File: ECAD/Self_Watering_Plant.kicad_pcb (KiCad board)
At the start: 2 copper layers, 65 parts, among them J1 Conn_01x02, J2 Conn_01x02, J3 Conn_01x02, J4 Conn_01x02, J5 Conn_01x02, J6 USB_A, J7 Conn_01x02, J8 Conn_01x02, J9 Conn_01x03, P1 U262-161N-4BVC11, Q1 BC817, Q2 BC817, Q3 NCE3018AS, Q4 NCE3018AS, Q5 NCE3018AS, Q6 NCE3018AS, Q7 NCE3018AS, Q8 NCE3018AS, Q9 TEPT4400, SW1 SW_Push, U1 LM293, U10 DHT11, U3 CH340C, U4 ESP32-WROOM-32, U5 NC7SB3157P6X, U6 NC7SB3157P6X, U7 NC7SB3157P6X, U8 LM293

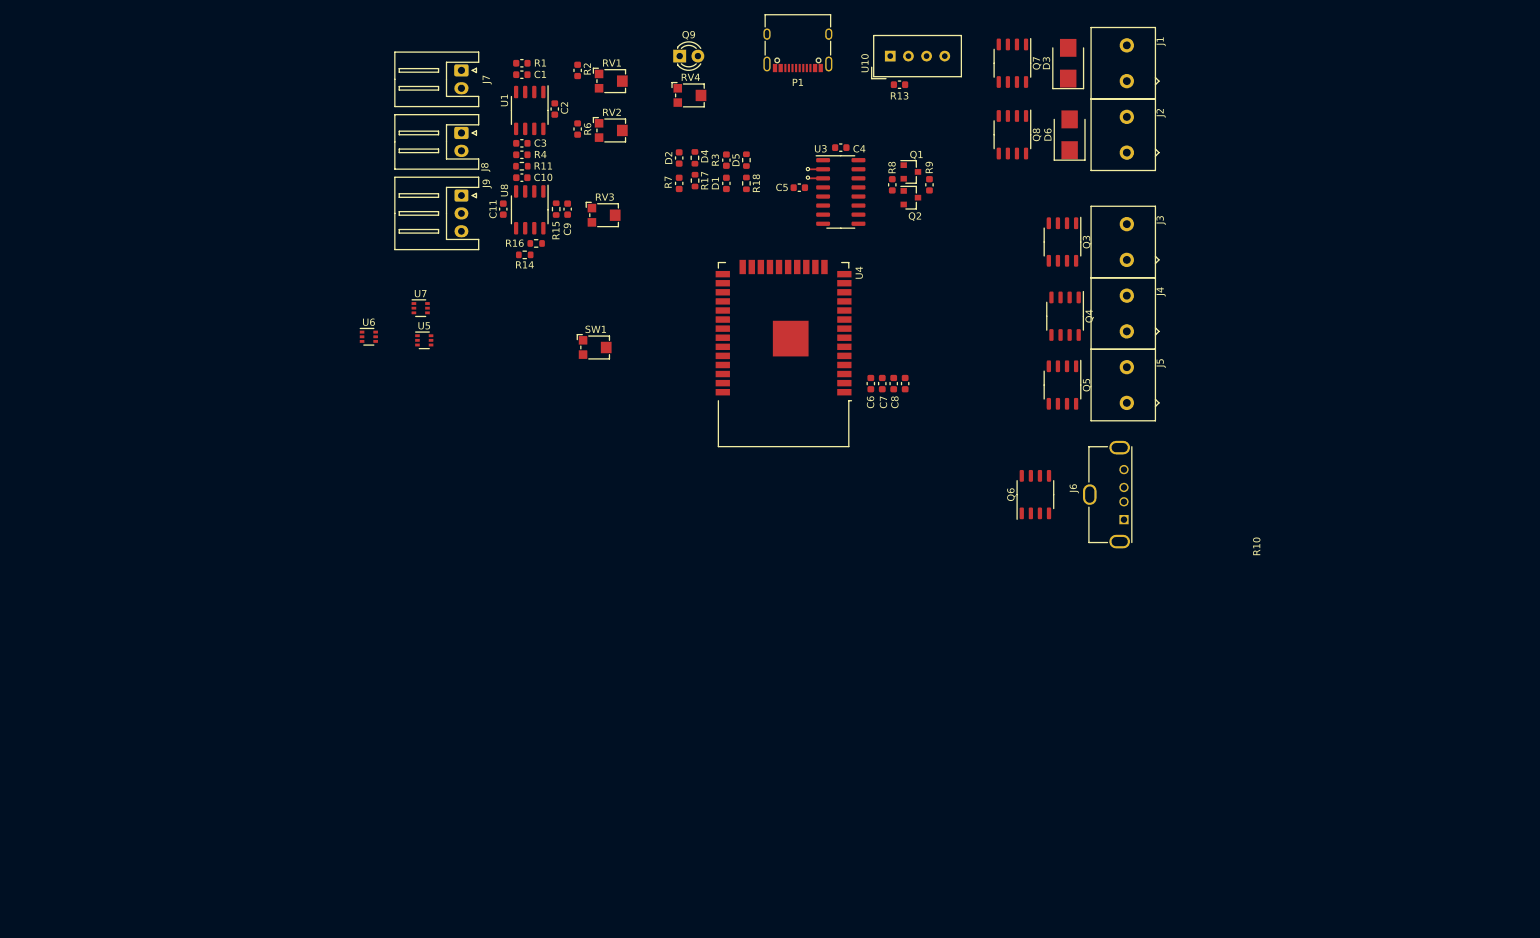
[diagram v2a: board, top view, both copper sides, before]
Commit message: finishing up pcb, only billonly bill of materials need to be done to be compatible with lc from jlcpcb
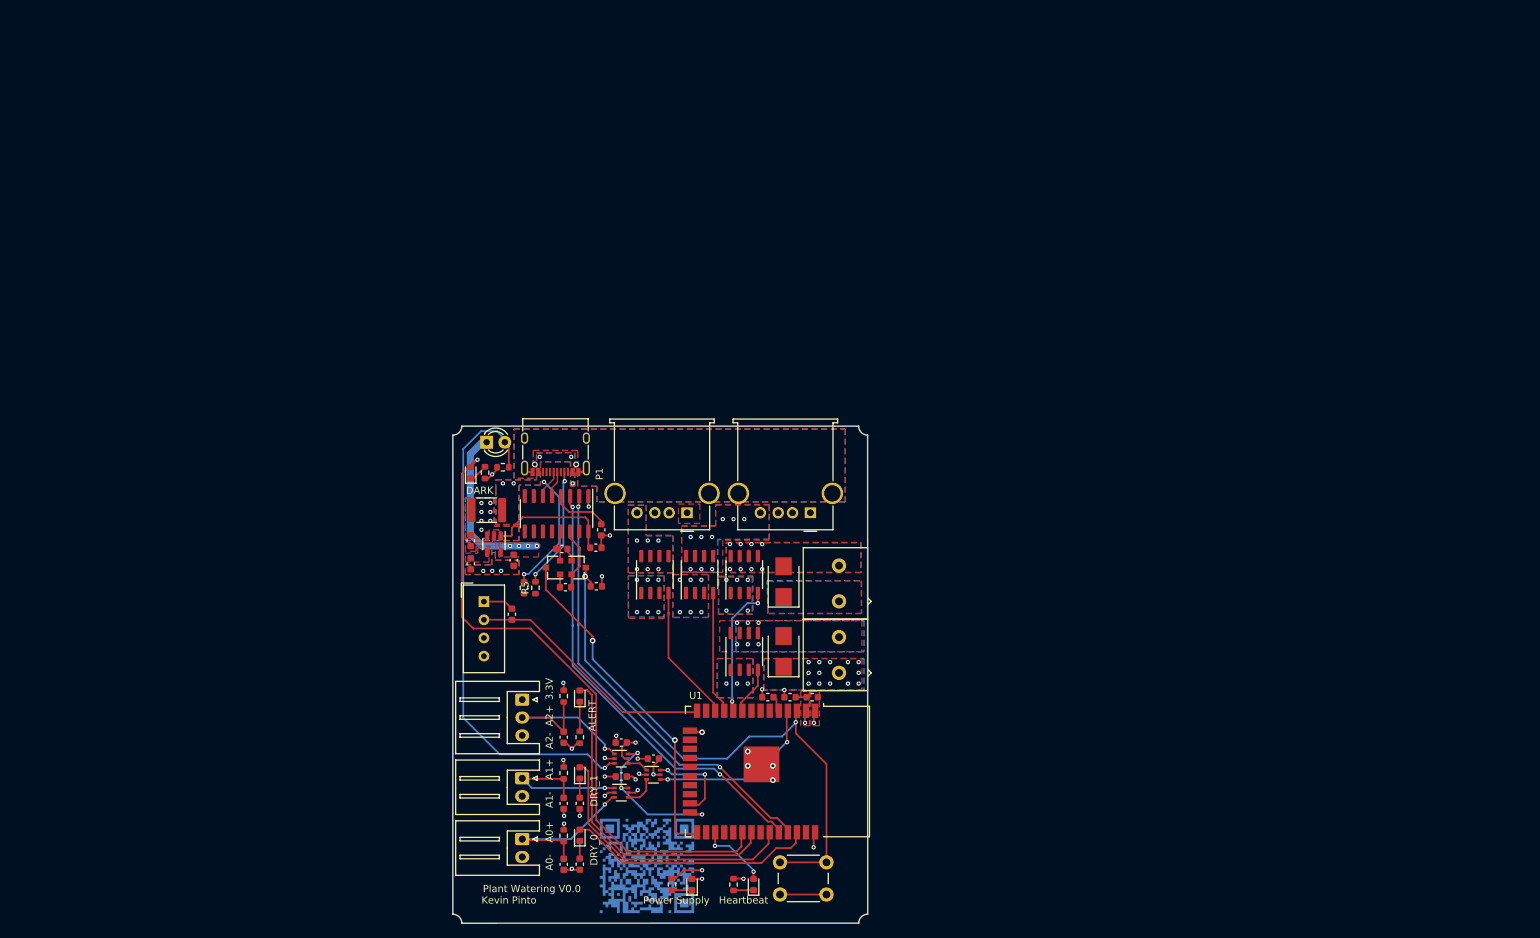
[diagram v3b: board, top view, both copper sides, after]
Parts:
- removed C10: 10nF, Capacitor_SMD:C_0603_1608Metric
- removed C2, C9: 100nF, Capacitor_SMD:C_0603_1608Metric
- removed J4, J5: Conn_01x02, ConnectorsSMD:TB001-500-02BE
- removed Q3, Q4, Q5, Q6, Q7, Q8: NCE3018AS, Package_SO:SOP-8_3.9x4.9mm_P1.27mm
- removed R15, R16: 10K, Resistor_SMD:R_0603_1608Metric
- removed RV1, RV2, RV3, RV4: 10K, Potentiometer_SMD:Potentiometer_Bourns_TC33X_Vertical
- removed U4: ESP32-WROOM-32, RF_Module:ESP32-WROOM-32
- removed U8: LM293, Package_SO:SO-8_3.9x4.9mm_P1.27mm
- added C12: 1uF, Capacitor_SMD:C_0603_1608Metric, F.Cu at (116.2, 86.8)
- added C13: 10nF, Capacitor_SMD:C_0603_1608Metric, F.Cu at (116.2, 90.0)
- added C14: 1uF, Capacitor_SMD:C_0603_1608Metric, F.Cu at (122.2, 89.5)
- added C15: 0.1uF, Capacitor_SMD:C_0603_1608Metric, F.Cu at (141.8, 117.2)
- added C16: 0.1uF, Capacitor_SMD:C_0603_1608Metric, F.Cu at (137.3, 119.8)
- added C17: 0.1uF, Capacitor_SMD:C_0603_1608Metric, F.Cu at (137.3, 115.0)
- added D7: NCD0603R1, LED_SMD:LED_0603_1608Metric, F.Cu at (147.2, 134.8)
- added D8: NCD0603R1, LED_SMD:LED_0603_1608Metric, F.Cu at (155.8, 134.8)
- added F1: Polyfuse_Small, Fuse:Fuse_1812_4532Metric, F.Cu at (118.5, 82.5)
- added R12: 1K, Resistor_SMD:R_0603_1608Metric, F.Cu at (153.0, 134.8)
- added R5: 5.1K, Resistor_SMD:R_0603_1608Metric, F.Cu at (125.3, 93.3)
- added REF**: PlantWateringQR, PlantWateringQR:PlantWateringQR, B.Cu at (141.0, 132.4)
- added U11: BCT2028, Package_TO_SOT_SMD:SOT-23-5, F.Cu at (119.5, 87.2)
- added U13: NCE3018AS, Package_SO:SO-8_3.9x4.9mm_P1.27mm, F.Cu at (142.0, 91.5)
- added U14: NCE3018AS, Package_SO:SO-8_3.9x4.9mm_P1.27mm, F.Cu at (148.2, 91.5)
- added U2: NCE3018AS, Package_SO:SO-8_3.9x4.9mm_P1.27mm, F.Cu at (154.5, 91.5)
- added U9: NCE3018AS, Package_SO:SO-8_3.9x4.9mm_P1.27mm, F.Cu at (154.5, 102.2)
- C4: value 10uF -> 0.1uF
- C5: value 0.1nF -> 0.1uF
- C8: value C_Small -> 0.1uF
- D1, D2, D4, D5: value LED -> NCD0603R1; footprint Resistor_SMD:R_0603_1608Metric -> LED_SMD:LED_0603_1608Metric
- J3: value Conn_01x02 -> USB_A; footprint ConnectorsSMD:TB001-500-02BE -> Connector_USB:USB_A_Molex_67643_Horizontal
- J6: footprint Connector_USB:USB_A_Molex_105057_Vertical -> Connector_USB:USB_A_Molex_67643_Horizontal
- R2: value 10K -> 5.1K
- R6: value 10K -> 1K
- R8, R9: value R_Small -> 10K
- SW1: footprint Potentiometer_SMD:Potentiometer_Bourns_TC33X_Vertical -> Button_Switch_THT:SW_PUSH_6mm_H4.3mm
- U1: value LM293 -> ESP32-WROOM-32; footprint Package_SO:SO-8_3.9x4.9mm_P1.27mm -> RF_Module:ESP32-WROOM-32
- moved R6 106.5 mm to (144.4, 134.8), turned to 90 degrees
- moved C1 102.1 mm to (129.2, 123.5), turned to -90 degrees
- moved C3 101.0 mm to (129.2, 132.0), turned to -90 degrees
- moved R3 100.6 mm to (131.5, 132.0), turned to -90 degrees
- moved R1 99.4 mm to (129.2, 119.2), turned to -90 degrees
- moved J7 99.4 mm to (123.5, 120.0)
- moved J8 99.1 mm to (123.5, 128.5)
- moved U1 97.7 mm to (156.2, 119.0)
- moved R4 95.4 mm to (129.2, 128.0), turned to -90 degrees
- moved U10 95.1 mm to (118.1, 95.3), turned to 0 degrees
- moved D1 93.4 mm to (131.5, 128.0), turned to 90 degrees
- moved R13 91.8 mm to (122.0, 97.0), turned to -90 degrees
- moved R7 87.8 mm to (131.5, 123.5)
- moved D2 87.1 mm to (131.5, 119.2)
- moved J1 83.1 mm to (167.8, 92.8)
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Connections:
- C1 pad 1: /AnalogMux/AIN_0 -> /AnalogMux/AIN_1
- C11 pad 1: /AnalogMux/AIN_3 -> /AnalogMux/AIN_2
- C3 pad 1: /AnalogMux/AIN_1 -> /AnalogMux/AIN_0
- D1 pad 2: +3V3 -> /ALERT0_IS_DRY
- D2 pad 2: +3V3 -> /ALERT1_IS_DRY
- D3 pad 1: VDD -> +5V
- D4 pad 2: +3V3 -> /ALERT2_IS_DARK
- D5 pad 2: +3V3 -> /ALERT3_CUSTOM
- D6 pad 1: VDD -> +5V
- D6 pad 2: /WATERPUM_B- -> /WaterPumpControl/WATERPUMP_B-
- J1 pad 1: VDD -> +5V
- J2 pad 1: VDD -> +5V
- J2 pad 2: /WATERPUM_B- -> /WaterPumpControl/WATERPUMP_B-
- J3 pad 1: VDD -> +5V
- J3 pad 2: /LedControl/LEDSTRIP_A- -> unconnected-(J3-Pad2)
- J6 pad 4: /LedControl/USB_LEDSTRIP_USB- -> /LedControl/USB_LED_A_N
- J7 pad 1: /AnalogMux/AIN_0 -> /AnalogMux/AIN_1
- J8 pad 1: /AnalogMux/AIN_1 -> /AnalogMux/AIN_0
- J9 pad 2: /AnalogMux/AIN_3 -> /AnalogMux/AIN_2
- P1 pad A4: +5V -> Net-(F1-Pad1)
- P1 pad A5: unconnected-(P1-PadA5) -> Net-(P1-PadA5)
- P1 pad A9: +5V -> Net-(F1-Pad1)
- P1 pad B4: +5V -> Net-(F1-Pad1)
- P1 pad B5: unconnected-(P1-PadB5) -> Net-(P1-PadB5)
- P1 pad B9: +5V -> Net-(F1-Pad1)
- Q9 pad 2: /AnalogMux/AIN_2 -> /AnalogMux/AIN_3
- R1 pad 2: /AnalogMux/AIN_0 -> /AnalogMux/AIN_1
- R11 pad 1: /AnalogMux/AIN_2 -> /AnalogMux/AIN_3
- R14 pad 2: /AnalogMux/AIN_3 -> /AnalogMux/AIN_2
- R17 pad 2: /ALERT2_IS_DARK -> GND
- R18 pad 2: /ALERT3_CUSTOM -> GND
- R2 pad 1: +3V3 -> GND
- R2 pad 2: /ALERT0_IS_DRY -> Net-(P1-PadB5)
- R3 pad 2: /ALERT0_IS_DRY -> GND
- R4 pad 2: /AnalogMux/AIN_1 -> /AnalogMux/AIN_0
- R6 pad 1: +3V3 -> Net-(D7-Pad1)
- R6 pad 2: /ALERT1_IS_DRY -> GND
- R7 pad 2: /ALERT1_IS_DRY -> GND
- U1 pad 1: /ALERT0_IS_DRY -> GND
- U1 pad 2: Net-(RV1-Pad2) -> +3V3
- U1 pad 3: /AnalogMux/AIN_0 -> /Controller/EN
- U1 pad 4: GND -> /AnalogMux/AOUT
- U1 pad 5: /AnalogMux/AIN_1 -> Net-(R10-Pad1)
- U1 pad 6: Net-(RV2-Pad2) -> unconnected-(U1-Pad6)
- U1 pad 7: /ALERT1_IS_DRY -> unconnected-(U1-Pad7)
- U1 pad 8: +3V3 -> unconnected-(U1-Pad8)
- U5 pad 1: unconnected-(U5-Pad1) -> /AnalogMux/AIN_1
- U5 pad 3: unconnected-(U5-Pad3) -> /AnalogMux/AIN_0
- U5 pad 4: unconnected-(U5-Pad4) -> Net-(U5-Pad4)
- U5 pad 6: unconnected-(U5-Pad6) -> /SEL0
- U6 pad 1: unconnected-(U6-Pad1) -> /AnalogMux/AIN_2
- U6 pad 2: unconnected-(U6-Pad2) -> GND
- U6 pad 3: unconnected-(U6-Pad3) -> /AnalogMux/AIN_3
- U6 pad 4: unconnected-(U6-Pad4) -> Net-(U6-Pad4)
- U6 pad 5: unconnected-(U6-Pad5) -> +3V3
- U6 pad 6: unconnected-(U6-Pad6) -> /SEL0
- U7 pad 1: unconnected-(U7-Pad1) -> Net-(U6-Pad4)
- U7 pad 2: /SEL0 -> GND
- U7 pad 3: unconnected-(U7-Pad3) -> Net-(U5-Pad4)
- U7 pad 5: unconnected-(U7-Pad5) -> +3V3
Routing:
- net /ALERT3_CUSTOM: track 0.00 -> 89.7 mm, vias 0 -> 1
- net /Controller/EN: track 0.00 -> 81.5 mm, vias 0 -> 2
- net /AnalogMux/AIN_3: track 0.00 -> 73.9 mm, vias 0 -> 1
- net /Controller/TX: track 2.14 -> 63.2 mm, vias 1 -> 2
- net /Controller/RX: track 2.16 -> 63.0 mm, vias 1 -> 2
- net GND: track 0.00 -> 48.1 mm, vias 0 -> 48
- net /Controller/IO0: track 0.00 -> 47.5 mm, vias 0 -> 2
- net +3V3: track 0.00 -> 46.5 mm, vias 0 -> 13
- net /ALERT2_IS_DARK: track 0.00 -> 45.9 mm
- net /ALERT1_IS_DRY: track 0.00 -> 38.3 mm
- net /Controller/DH11_IO: track 0.00 -> 35.0 mm
- net /ALERT0_IS_DRY: track 0.00 -> 34.7 mm
- net /AnalogMux/AIN_2: track 0.00 -> 27.4 mm, vias 0 -> 1
- net /AnalogMux/AOUT: track 0.00 -> 24.1 mm, vias 0 -> 2
- net /AnalogMux/AIN_0: track 0.00 -> 23.7 mm, vias 0 -> 1
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- added copper zone on F.Cu, net +3V3
- added copper zone on In2.Cu, net +3V3
- added copper zone on B.Cu, net +5V
- added copper zone on F.Cu, net +5V
- added copper zone on In2.Cu, net +5V
- added copper zone on B.Cu, net /LedControl/USB_LED_A_N
- added copper zone on F.Cu, net /LedControl/USB_LED_A_N
- added copper zone on B.Cu, net /LedControl/USB_LED_B_N
- added copper zone on F.Cu, net /LedControl/USB_LED_B_N
- added copper zone on B.Cu, net /WaterPumpControl/WATERPUMP_A-
- added copper zone on F.Cu, net /WaterPumpControl/WATERPUMP_A-
- added copper zone on B.Cu, net /WaterPumpControl/WATERPUMP_B-
- added copper zone on F.Cu, net /WaterPumpControl/WATERPUMP_B-
- added copper zone on B.Cu, net GND
- added copper zone on F.Cu, net GND
- added copper zone on In1.Cu, net GND
- added copper zone on F.Cu, net Net-(C13-Pad1)
- added copper zone on B.Cu, net Net-(F1-Pad1)
- added copper zone on F.Cu, net Net-(F1-Pad1)
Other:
- board outline added: 58 x 69.5 mm
- copper layers 2 -> 4
- board text added: "3.3V"
- board text added: "A0+"
- board text added: "A0-"
- board text added: "A1+"
- board text added: "A1-"
- board text added: "A2+"
- board text added: "A2-"
- board text added: "ALERT"
- board text added: "DARK"
- board text added: "DRY_0"
- board text added: "DRY_1"
- board text added: "Heartbeat"
- board text added: "Kevin Pinto"
- board text added: "Plant Watering V0.0"
- board text added: "Power Supply"

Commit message: BOM fixed, ready to order
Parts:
- removed REF**: PlantWateringQR, PlantWateringQR:PlantWateringQR
- moved U1 0.20 mm to (156.2, 119.2)
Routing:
- net GND: track 48.1 -> 51.3 mm, vias 48 -> 49
- net Net-(P1-PadB5): track 17.2 -> 18.7 mm
- net /WaterPumpControl/WATERPUMP_B-: vias 6 -> 17
- net /WaterPumpControl/WATERPUMP_A-: vias 8 -> 19
- net +5V: vias 20 -> 31
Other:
- board text added: "HB"
- board text added: "HEALTH"
- board text added: "LEDA"
- board text added: "LEDB"
- board text added: "UART"
- board text added: "WPA+"
- board text added: "WPA-"
- board text added: "WPB+"
- board text added: "WPB-"
- board text removed: "Heartbeat"
- board text removed: "Power Supply"

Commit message: adding production and step files
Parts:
- removed U10: DHT11, Sensor:Aosong_DHT11_5.5x12.0_P2.54mm
- added C2: 10uF, Capacitor_SMD:C_0603_1608Metric, F.Cu at (136.7, 102.2)
- added G***: LOGO, Symbols:heartbeat, F.Cu at (155.7, 137.6)
- added G***: LOGO, Symbols:plant, F.Cu at (135.2, 135.7)
- added R15: 5.1K, Resistor_SMD:R_0603_1608Metric, F.Cu at (141.7, 100.7)
- added REF**: OSHW-Logo_5.7x6mm_SilkScreen, Symbol:OSHW-Logo_5.7x6mm_SilkScreen, F.Cu at (140.8, 135.4)
- added U4: AHT20, Package_DFN:SOIC-6, F.Cu at (139.1, 102.2)
- P1: value U262-161N-4BVC11 -> C-31-M-12; footprint Connector_USB:USB_C_Receptacle_XKB_U262-16XN-4BVC11 -> Connector_USB:USB_C_Receptacle_HRO_TYPE-C-31-M-12
- R13: value 10K -> 5.1K
- moved R13 20.8 mm to (141.7, 103.8)
- moved R6 1.15 mm to (145.6, 134.8)
- moved R5 0.45 mm to (124.8, 93.3)
- moved R2 0.40 mm to (123.3, 93.3)
- moved Q1 0.25 mm to (131.6, 90.5)
- moved Q2 0.10 mm to (127.7, 90.5)
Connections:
- R13 pad 2: /Controller/DH11_IO -> /Controller/SCL
- U1 pad 13: unconnected-(U1-Pad13) -> /Controller/CTRL_WATERPUMP_B
- U1 pad 14: /Controller/DH11_IO -> unconnected-(U1-Pad14)
- U1 pad 8: unconnected-(U1-Pad8) -> /Controller/SCL
- U1 pad 9: /Controller/CTRL_WATERPUMP_B -> /Controller/SDA
- U3 pad 2: /Controller/TX -> /Controller/RX
- U3 pad 3: /Controller/RX -> /Controller/TX
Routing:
- net /Controller/DH11_IO: track 35.0 -> 0.00 mm
- net /Controller/SDA: track 0.00 -> 24.5 mm, vias 0 -> 2
- net /Controller/SCL: track 0.00 -> 24.1 mm, vias 0 -> 2
- net Net-(Q1-Pad2): track 9.13 -> 18.7 mm
- net +3V3: track 46.5 -> 52.9 mm, vias 13 -> 14
- net /ALERT3_CUSTOM: track 89.7 -> 84.5 mm, vias 1 -> 0
- net /Controller/CTRL_WATERPUMP_B: track 6.88 -> 12.0 mm, vias 0 -> 2
- net /Controller/EN: track 81.5 -> 85.5 mm
- net /Controller/RX: track 63.0 -> 64.5 mm
- net GND: track 51.3 -> 52.6 mm, vias 49 -> 51
- net Net-(D7-Pad1): track 2.82 -> 1.66 mm
- net +5V: track 18.0 -> 17.4 mm
- net Net-(C5-Pad1): track 8.17 -> 8.75 mm
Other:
- board text added: "ON"
- board text added: "RESET"
- board text removed: "HB"
- board text removed: "HEALTH"
